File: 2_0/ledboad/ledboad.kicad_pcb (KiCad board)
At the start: 2 copper layers, 96 x 34.2 mm, 333 parts, among them J1 Conn_02x05_Odd_Even, Q1 AO3401A, Q2 AO3401A, Q3 AO3401A, Q4 AO3401A, Q5 AO3401A, Q6 AO3401A, Q7 AO3401A, Q8 AO3401A, SW1 RST, U1 STM32G070CBTx, U2 XC6206PxxxMR, Y1 2016/DNP

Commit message: save before next rev
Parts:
- added REF**: pilkbrain, Critbit_lib:pilkbrain, B.Cu at (62.0, 31.1)

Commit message: commit before rescheme
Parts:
- removed C1, C3: 100n, Capacitor_SMD:C_0402_1005Metric
- removed C2, C4: 470n, Capacitor_SMD:C_0402_1005Metric
- removed C7, C8: 10p/DNP, Capacitor_SMD:C_0402_1005Metric
- removed REF**: pilkbrain, Critbit_lib:pilkbrain
- removed SW1: RST, Button_Switch_SMD:SW_SPST_FSMSM
- removed TP1, TP10, TP11, TP12, TP13, TP14, TP15, TP16, TP17, TP18, TP19, TP2, TP20, TP21, TP22, TP23, TP24, TP25, TP26, TP27, TP28, TP29, TP3, TP30, TP31, TP32, TP4, TP5, TP6, TP7, TP8, TP9: TP, TestPoint:TestPoint_Pad_D1.0mm
- removed U1: STM32G070CBTx, Package_QFP:LQFP-48_7x7mm_P0.5mm
- removed Y1: 2016/DNP, Crystal:Crystal_SMD_2016-4Pin_2.0x1.6mm
- added R18: 5.1k, Resistor_SMD:R_0201_0603Metric, F.Cu at (93.7, 53.6)
- added R19: 5.1k, Resistor_SMD:R_0201_0603Metric, F.Cu at (91.8, 53.6)
- added U3: ~, Critbit_lib:pilkbrain, B.Cu at (55.8, 32.2)
- J1: value Conn_02x05_Odd_Even -> USB_C_Receptacle_USB2.0; footprint Critbit_lib:YXT-BB10-10S -> Connector_USB:USB_C_Receptacle_HRO_TYPE-C-31-M-12; moved to F.Cu
- U2: value XC6206PxxxMR -> 74HC138PW,118; footprint Package_TO_SOT_SMD:SOT-23-3 -> easyeda2kicad:SSOP-16_L6.2-W5.3-P0.65-LS7.8-BL
- moved J1 33.2 mm to (93.0, 46.4)
- moved U2 30.7 mm to (58.6, 55.8), turned to 0 degrees
- moved C5 8.66 mm to (72.0, 56.8), turned to 90 degrees
- moved C10 1.46 mm to (137.8, 48.6)
- moved D0_1 1.46 mm to (46.5, 17.9)
- moved D0_2 1.46 mm to (46.5, 20.8)
- moved D0_3 1.46 mm to (46.5, 23.8)
- moved D0_4 1.46 mm to (46.5, 26.8)
- moved D0_5 1.46 mm to (46.5, 29.8)
- moved D0_6 1.46 mm to (46.5, 32.8)
- moved D0_7 1.46 mm to (46.5, 35.8)
- moved D0_8 1.46 mm to (46.5, 38.8)
- moved D1 1.46 mm to (100.2, 46.0)
- moved D10_1 1.46 mm to (76.5, 17.9)
- moved D10_2 1.46 mm to (76.5, 20.8)
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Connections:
- RU6 pad 22: /DAT6 -> unconnected-(RU6-SDO-Pad22)
- U2 pad 1: GND -> /MATRIX_A
- U2 pad 2: +3V3 -> /MATRIX_B
- U2 pad 3: VDD -> /MATRIX_C
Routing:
- net /ROW_0_CTRL: track 67.2 -> 4.86 mm, vias 2 -> 1
- net /WS2812_DAT: track 45.1 -> 0.00 mm, vias 3 -> 0
- net VDD: track 195.9 -> 154.4 mm, vias 18 -> 15
- net /DAT0: track 44.2 -> 4.32 mm, vias 0 -> 1
- net /ROW_1_CTRL: track 46.5 -> 6.93 mm
- net GND: track 46.7 -> 21.0 mm, vias 17 -> 9
- net /OE: track 125.2 -> 100.4 mm, vias 12 -> 8
- net /LAT: track 119.6 -> 95.2 mm, vias 14 -> 11
- net /SCLK: track 93.6 -> 73.9 mm
- net /ROW_2_CTRL: track 24.9 -> 5.50 mm, vias 2 -> 0
- net /DM: track 0.00 -> 15.2 mm, vias 0 -> 2
- net /STM_NRST: track 14.2 -> 0.00 mm, vias 4 -> 0
- net +3V3: track 11.0 -> 0.00 mm, vias 1 -> 0
- net /ROW_3_CTRL: track 60.2 -> 50.3 mm, vias 4 -> 3
- net /STM_LEDB: track 9.66 -> 0.00 mm, vias 2 -> 0
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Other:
- board size 96 x 34.2 mm -> 100 x 32 mm
- board text added: "10.2024"
- board text added: "Cyberbadge 2.1"
- board text removed: "07.2023"
- board text removed: "Cyberbadge 2.0 prototype"
- board text removed: "D0 | LAT | 4x ext"
- board text removed: "D1"
- board text removed: "DAT2"
- board text removed: "DAT5"
- board text removed: "DAT6"
- board text removed: "GND"
- board text removed: "LAT | SCLK"
- board text removed: "OE"
- board text removed: "SPI2_MOSI | SPI2_MISO | OE | SPI2_SCLK"
- board text removed: "SPI2_NSS | SCLK | GND | ADC"
- board text removed: "SWCLK | SWDIO | GND | nRST | 3v3 | VDD | DAT3"
- board text removed: "TX | RX"

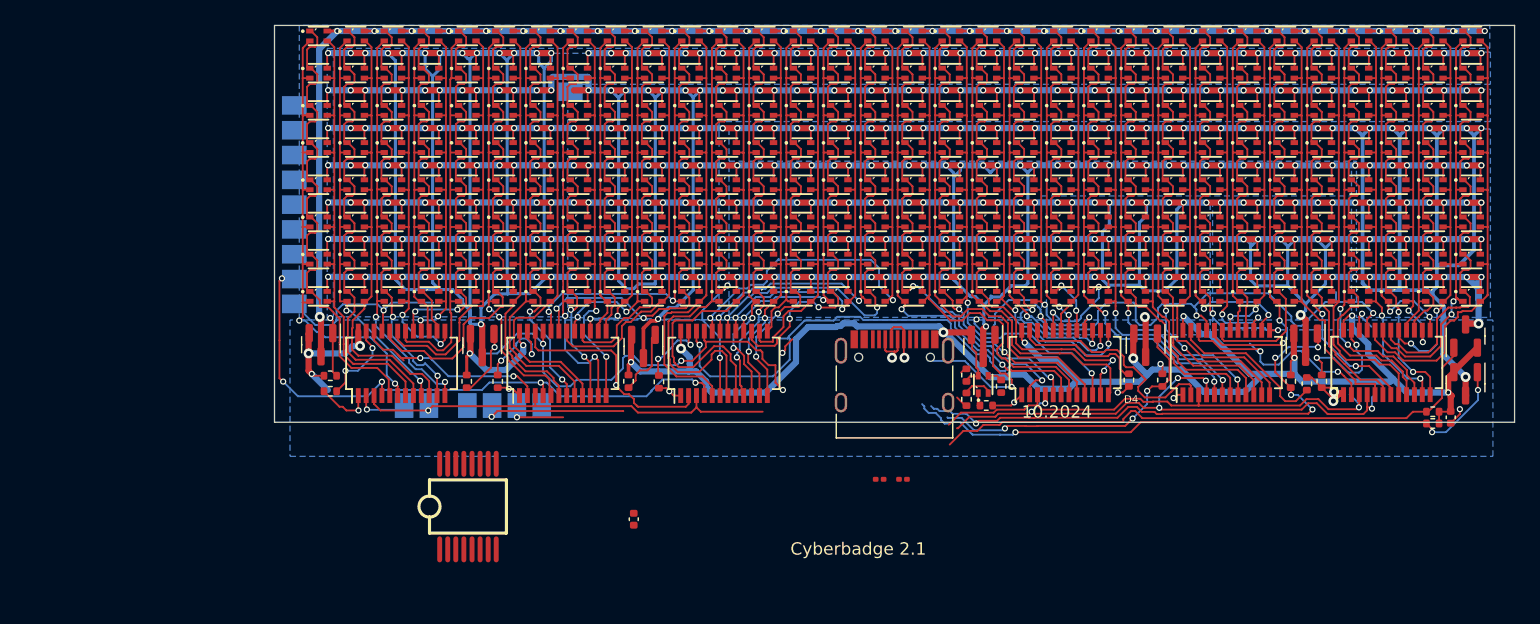
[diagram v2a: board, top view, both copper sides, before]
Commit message: rescheme, reroute
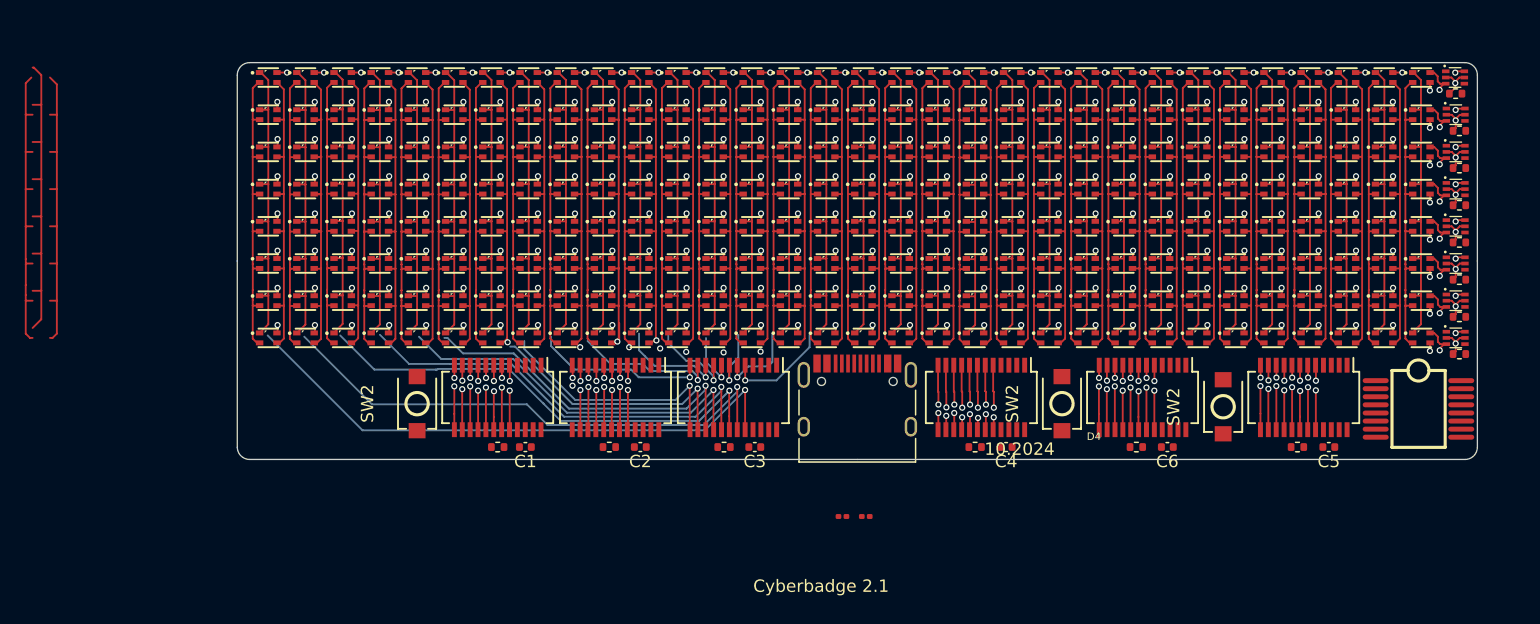
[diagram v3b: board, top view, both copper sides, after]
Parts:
- removed C10: 470n, Capacitor_SMD:C_0402_1005Metric
- removed D1: LED_RGBA, Critbit_lib:0606
- removed Q1, Q2, Q3, Q4, Q5, Q6, Q7, Q8: AO3401A, Package_TO_SOT_SMD:SOT-23
- removed R1, R2, R3, R4, R5, R6, R7, R8: 10k, Resistor_SMD:R_0402_1005Metric
- removed U3: ~, Critbit_lib:pilkbrain
- added C1: 470n, Capacitor_SMD:C_0402_1005Metric, F.Cu at (63.2, 51.0)
- added C2: 470n, Capacitor_SMD:C_0402_1005Metric, F.Cu at (72.5, 51.0)
- added C3: 470n, Capacitor_SMD:C_0402_1005Metric, F.Cu at (81.7, 51.0)
- added C4: 470n, Capacitor_SMD:C_0402_1005Metric, F.Cu at (102.0, 51.0)
- added C6: 470n, Capacitor_SMD:C_0402_1005Metric, F.Cu at (115.0, 51.0)
- added Q10: CJX3139K, easyeda2kicad:SOT-563_L1.6-W1.2-P0.50-LS1.6-BR, F.Cu at (138.2, 24.2)
- added Q11: CJX3139K, easyeda2kicad:SOT-563_L1.6-W1.2-P0.50-LS1.6-BR, F.Cu at (138.2, 27.2)
- added Q12: CJX3139K, easyeda2kicad:SOT-563_L1.6-W1.2-P0.50-LS1.6-BR, F.Cu at (138.2, 30.2)
- added Q13: CJX3139K, easyeda2kicad:SOT-563_L1.6-W1.2-P0.50-LS1.6-BR, F.Cu at (138.2, 33.2)
- added Q14: CJX3139K, easyeda2kicad:SOT-563_L1.6-W1.2-P0.50-LS1.6-BR, F.Cu at (138.2, 36.2)
- added Q15: CJX3139K, easyeda2kicad:SOT-563_L1.6-W1.2-P0.50-LS1.6-BR, F.Cu at (138.2, 39.2)
- added Q16: CJX3139K, easyeda2kicad:SOT-563_L1.6-W1.2-P0.50-LS1.6-BR, F.Cu at (138.2, 42.2)
- added Q9: CJX3139K, easyeda2kicad:SOT-563_L1.6-W1.2-P0.50-LS1.6-BR, F.Cu at (138.2, 21.2)
- added R20: 10k, Resistor_SMD:R_0402_1005Metric, F.Cu at (138.6, 31.5)
- added R21: 10k, Resistor_SMD:R_0402_1005Metric, F.Cu at (138.6, 34.5)
- added R22: 10k, Resistor_SMD:R_0402_1005Metric, F.Cu at (138.6, 37.5)
- added R23: 10k, Resistor_SMD:R_0402_1005Metric, F.Cu at (138.6, 40.5)
- added R24: 10k, Resistor_SMD:R_0402_1005Metric, F.Cu at (138.6, 43.5)
- added SW2: TS-1088-AR02016, easyeda2kicad:SW-SMD_L3.9-W3.0-P4.45, F.Cu at (54.5, 47.5)
- added SW2: TS-1088-AR02016, easyeda2kicad:SW-SMD_L3.9-W3.0-P4.45, F.Cu at (119.5, 47.8)
- added SW2: TS-1088-AR02016, easyeda2kicad:SW-SMD_L3.9-W3.0-P4.45, F.Cu at (106.5, 47.5)
- moved R9 78.1 mm to (125.5, 51.0), turned to 0 degrees
- moved U2 77.1 mm to (135.2, 47.9), turned to -90 degrees
- moved RU1 72.8 mm to (126.0, 47.0), turned to -90 degrees
- moved RU6 71.8 mm to (61.0, 47.0), turned to -90 degrees
- moved R14 66.7 mm to (61.0, 51.0), turned to 0 degrees
- moved R12 56.5 mm to (70.0, 51.0), turned to 0 degrees
- moved C5 56.4 mm to (128.0, 51.0), turned to 180 degrees
- moved R11 51.8 mm to (112.5, 51.0), turned to 0 degrees
- moved RU4 49.3 mm to (70.5, 47.0), turned to -90 degrees
- moved RU3 46.8 mm to (113.0, 47.0), turned to -90 degrees
- moved R15 45.4 mm to (138.2, 22.5), turned to 180 degrees
- moved R16 45.3 mm to (138.6, 25.5), turned to 180 degrees
- moved R17 40.9 mm to (138.6, 28.5), turned to 180 degrees
- moved R10 33.1 mm to (79.2, 51.0), turned to 0 degrees
- moved RU2 26.9 mm to (80.0, 47.0), turned to -90 degrees
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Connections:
- R15 pad 1: Net-(D1-RK) -> VDD
- R15 pad 2: GND -> /ROW_0_CTRL
- R16 pad 1: Net-(D1-GK) -> VDD
- R16 pad 2: /STM_LEDG -> /ROW_1_CTRL
- R17 pad 1: Net-(D1-BK) -> VDD
- R17 pad 2: /STM_LEDB -> /ROW_2_CTRL
- RU1 pad 10: /COL_B1 -> /COL_R26
- RU1 pad 11: /COL_R2 -> /COL_R25
- RU1 pad 12: /COL_G2 -> /COL_R24
- RU1 pad 13: /COL_B2 -> /COL_R23
- RU1 pad 14: /COL_R3 -> /COL_R22
- RU1 pad 15: /COL_G3 -> /COL_R21
- RU1 pad 16: /COL_B3 -> /COL_R20
- RU1 pad 17: /COL_R4 -> /COL_R19
- RU1 pad 18: /COL_G4 -> /COL_R18
- RU1 pad 19: /COL_B4 -> /COL_R17
- RU1 pad 2: /DAT0 -> /DAT_R
- RU1 pad 20: /COL_R5 -> /COL_R16
- RU1 pad 22: /DAT1 -> Net-(RU1-SDO)
- RU1 pad 5: /COL_R0 -> /COL_R31
- RU1 pad 6: /COL_G0 -> /COL_R30
- RU1 pad 7: /COL_B0 -> /COL_R29
- RU1 pad 8: /COL_R1 -> /COL_R28
- RU1 pad 9: /COL_G1 -> /COL_R27
- RU2 pad 10: /COL_B17 -> /COL_R10
- RU2 pad 11: /COL_R18 -> /COL_R9
- RU2 pad 12: /COL_G18 -> /COL_R8
- RU2 pad 13: /COL_B18 -> /COL_R7
- RU2 pad 14: /COL_R19 -> /COL_R6
- RU2 pad 15: /COL_G19 -> /COL_R5
- RU2 pad 16: /COL_B19 -> /COL_R4
- RU2 pad 17: /COL_R20 -> /COL_R3
- RU2 pad 18: /COL_G20 -> /COL_R2
- RU2 pad 19: /COL_B20 -> /COL_R1
- RU2 pad 2: /DAT3 -> Net-(RU1-SDO)
- RU2 pad 20: /COL_R21 -> /COL_R0
- RU2 pad 22: /DAT4 -> unconnected-(RU2-SDO-Pad22)
- RU2 pad 5: /COL_R16 -> /COL_R15
- RU2 pad 6: /COL_G16 -> /COL_R14
- RU2 pad 7: /COL_B16 -> /COL_R13
- RU2 pad 8: /COL_R17 -> /COL_R12
- RU2 pad 9: /COL_G17 -> /COL_R11
- RU3 pad 10: /COL_R7 -> /COL_G26
- RU3 pad 11: /COL_G7 -> /COL_G25
- RU3 pad 12: /COL_B7 -> /COL_G24
- RU3 pad 13: /COL_R8 -> /COL_G23
- RU3 pad 14: /COL_G8 -> /COL_G22
- RU3 pad 15: /COL_B8 -> /COL_G21
- RU3 pad 16: /COL_R9 -> /COL_G20
- RU3 pad 17: /COL_G9 -> /COL_G19
- RU3 pad 18: /COL_B9 -> /COL_G18
- RU3 pad 19: /COL_R10 -> /COL_G17
- RU3 pad 2: /DAT1 -> /DAT_G
- RU3 pad 20: /COL_G10 -> /COL_G16
- RU3 pad 22: /DAT2 -> Net-(RU3-SDO)
- RU3 pad 5: /COL_G5 -> /COL_G31
- RU3 pad 6: /COL_B5 -> /COL_G30
- RU3 pad 7: /COL_R6 -> /COL_G29
- RU3 pad 8: /COL_G6 -> /COL_G28
- RU3 pad 9: /COL_B6 -> /COL_G27
- RU4 pad 10: /COL_R23 -> /COL_G10
- RU4 pad 11: /COL_G23 -> /COL_G9
- RU4 pad 12: /COL_B23 -> /COL_G8
- RU4 pad 13: /COL_R24 -> /COL_G7
- RU4 pad 14: /COL_G24 -> /COL_G6
- RU4 pad 15: /COL_B24 -> /COL_G5
- RU4 pad 16: /COL_R25 -> /COL_G4
- RU4 pad 17: /COL_G25 -> /COL_G3
- RU4 pad 18: /COL_B25 -> /COL_G2
- RU4 pad 19: /COL_R26 -> /COL_G1
- RU4 pad 2: /DAT4 -> Net-(RU3-SDO)
- RU4 pad 20: /COL_G26 -> /COL_G0
- RU4 pad 22: /DAT5 -> unconnected-(RU4-SDO-Pad22)
- RU4 pad 5: /COL_G21 -> /COL_G15
- RU4 pad 6: /COL_B21 -> /COL_G14
- RU4 pad 7: /COL_R22 -> /COL_G13
- RU4 pad 8: /COL_G22 -> /COL_G12
- RU4 pad 9: /COL_B22 -> /COL_G11
- RU5 pad 10: /COL_G12 -> /COL_B26
- RU5 pad 11: /COL_B12 -> /COL_B25
- RU5 pad 12: /COL_R13 -> /COL_B24
- RU5 pad 13: /COL_G13 -> /COL_B23
- RU5 pad 14: /COL_B13 -> /COL_B22
- RU5 pad 15: /COL_R14 -> /COL_B21
- RU5 pad 16: /COL_G14 -> /COL_B20
- RU5 pad 17: /COL_B14 -> /COL_B19
- RU5 pad 18: /COL_R15 -> /COL_B18
- RU5 pad 19: /COL_G15 -> /COL_B17
- RU5 pad 2: /DAT2 -> /DAT_B
- RU5 pad 20: /COL_B15 -> /COL_B16
- RU5 pad 22: /DAT3 -> Net-(RU5-SDO)
- RU5 pad 5: /COL_B10 -> /COL_B31
- RU5 pad 6: /COL_R11 -> /COL_B30
- RU5 pad 7: /COL_G11 -> /COL_B29
- RU5 pad 8: /COL_B11 -> /COL_B28
- RU5 pad 9: /COL_R12 -> /COL_B27
- RU6 pad 10: /COL_G28 -> /COL_B10
- RU6 pad 11: /COL_B28 -> /COL_B9
- RU6 pad 12: /COL_R29 -> /COL_B8
- RU6 pad 13: /COL_G29 -> /COL_B7
- RU6 pad 14: /COL_B29 -> /COL_B6
- RU6 pad 15: /COL_R30 -> /COL_B5
- RU6 pad 16: /COL_G30 -> /COL_B4
- RU6 pad 17: /COL_B30 -> /ROW_7
- RU6 pad 18: /COL_R31 -> /COL_B2
- RU6 pad 19: /COL_G31 -> /COL_B1
- RU6 pad 2: /DAT5 -> Net-(RU5-SDO)
- RU6 pad 20: /COL_B31 -> /COL_B0
- RU6 pad 5: /COL_B26 -> /COL_B15
- RU6 pad 6: /COL_R27 -> /COL_B14
- RU6 pad 7: /COL_G27 -> /COL_B13
- RU6 pad 8: /COL_B27 -> /COL_B12
- RU6 pad 9: /COL_R28 -> /COL_B11
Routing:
- net /ROW_1: track 251.3 -> 23.1 mm, vias 63 -> 33
- net /ROW_3: track 203.5 -> 23.1 mm, vias 64 -> 33
- net /ROW_2: track 195.0 -> 23.1 mm, vias 63 -> 33
- net VDD: track 154.4 -> 0.00 mm, vias 15 -> 0
- net /ROW_4: track 166.5 -> 23.1 mm, vias 64 -> 33
- net /ROW_5: track 161.1 -> 23.1 mm, vias 64 -> 33
- net /ROW_6: track 158.0 -> 23.1 mm, vias 64 -> 33
- net /ROW_0: track 145.4 -> 27.2 mm
- net /OE: track 100.4 -> 0.00 mm, vias 8 -> 0
- net /ROW_7: track 138.5 -> 40.6 mm, vias 64 -> 34
- net /LAT: track 95.2 -> 0.00 mm, vias 11 -> 0
- net /SCLK: track 73.9 -> 0.00 mm, vias 2 -> 0
- net /COL_R0: track 40.6 -> 97.8 mm, vias 0 -> 1
- net /COL_G0: track 38.9 -> 85.6 mm, vias 2 -> 1
- net /DAT3: track 39.9 -> 0.00 mm, vias 2 -> 0
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- added copper zone on In1.Cu, net /ROW_0
- added copper zone on In1.Cu, net /ROW_1
- added copper zone on In1.Cu, net /ROW_2
- added copper zone on In1.Cu, net /ROW_3
- added copper zone on In1.Cu, net /ROW_4
- added copper zone on In1.Cu, net /ROW_5
- added copper zone on In1.Cu, net /ROW_6
- added copper zone on In1.Cu, net /ROW_7
- removed copper zone on B.Cu, net /ROW_0
- removed copper zone on B.Cu, net /ROW_1
- removed copper zone on B.Cu, net /ROW_2
- removed copper zone on B.Cu, net /ROW_3
- removed copper zone on B.Cu, net /ROW_4
- removed copper zone on B.Cu, net /ROW_5
- removed copper zone on B.Cu, net /ROW_6
- removed copper zone on B.Cu, net GND
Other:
- outline, holes or cut-outs redrawn
- copper layers 2 -> 4

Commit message: work on ledboard
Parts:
- removed the SW2 at (54.5, 47.5)
- removed the SW2 at (119.5, 47.8)
- added C7: 470n, Capacitor_SMD:C_0402_1005Metric, F.Cu at (138.9, 43.6)
- added SW1: TS-1088-AR02016, easyeda2kicad:SW-SMD_L3.9-W3.0-P4.45, F.Cu at (119.5, 47.3)
- added SW3: TS-1088-AR02016, easyeda2kicad:SW-SMD_L3.9-W3.0-P4.45, F.Cu at (51.9, 47.0)
- added U1: ~, Critbit_lib:pilkbrain2, B.Cu at (53.4, 38.8)
- R18, R19: footprint Resistor_SMD:R_0201_0603Metric -> Resistor_SMD:R_0402_1005Metric
- moved C5 33.6 mm to (95.3, 43.5)
- moved C6 16.5 mm to (131.5, 50.2), turned to 0 degrees
- moved R18 14.2 mm to (84.2, 44.0), turned to -90 degrees
- moved R19 11.6 mm to (84.2, 45.9), turned to 90 degrees
- moved R9 9.53 mm to (131.5, 43.6)
- moved R11 9.44 mm to (118.6, 43.8)
- moved R13 9.44 mm to (105.6, 43.8)
- moved C4 9.06 mm to (107.5, 43.8)
- moved R10 7.81 mm to (73.8, 45.4), turned to 90 degrees
- moved R24 6.70 mm to (138.8, 50.2)
- moved R12 5.23 mm to (73.8, 47.4), turned to -90 degrees
- moved R14 4.15 mm to (63.2, 47.5), turned to -90 degrees
- moved RU6 3.00 mm to (58.0, 47.0)
- moved C3 2.84 mm to (84.2, 49.6), turned to 90 degrees
- moved C2 2.06 mm to (73.8, 49.4), turned to 90 degrees
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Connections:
- RU1 pad 10: /COL_R26 -> /COL_R21
- RU1 pad 11: /COL_R25 -> /COL_R22
- RU1 pad 12: /COL_R24 -> /COL_R23
- RU1 pad 13: /COL_R23 -> /COL_R24
- RU1 pad 14: /COL_R22 -> /COL_R25
- RU1 pad 15: /COL_R21 -> /COL_R26
- RU1 pad 16: /COL_R20 -> /COL_R27
- RU1 pad 17: /COL_R19 -> /COL_R28
- RU1 pad 18: /COL_R18 -> /COL_R29
- RU1 pad 19: /COL_R17 -> /COL_R30
- RU1 pad 2: /DAT_R -> Net-(RU1-SDI)
- RU1 pad 20: /COL_R16 -> /COL_R31
- RU1 pad 22: Net-(RU1-SDO) -> unconnected-(RU1-SDO-Pad22)
- RU1 pad 5: /COL_R31 -> /COL_R16
- RU1 pad 6: /COL_R30 -> /COL_R17
- RU1 pad 7: /COL_R29 -> /COL_R18
- RU1 pad 8: /COL_R28 -> /COL_R19
- RU1 pad 9: /COL_R27 -> /COL_R20
- RU2 pad 10: /COL_R10 -> /COL_R5
- RU2 pad 11: /COL_R9 -> /COL_R6
- RU2 pad 12: /COL_R8 -> /COL_R7
- RU2 pad 13: /COL_R7 -> /COL_R8
- RU2 pad 14: /COL_R6 -> /COL_R9
- RU2 pad 15: /COL_R5 -> /COL_R10
- RU2 pad 16: /COL_R4 -> /COL_R11
- RU2 pad 17: /COL_R3 -> /COL_R12
- RU2 pad 18: /COL_R2 -> /COL_R13
- RU2 pad 19: /COL_R1 -> /COL_R14
- RU2 pad 2: Net-(RU1-SDO) -> /DAT_R
- RU2 pad 20: /COL_R0 -> /COL_R15
- RU2 pad 22: unconnected-(RU2-SDO-Pad22) -> Net-(RU1-SDI)
- RU2 pad 5: /COL_R15 -> /COL_R0
- RU2 pad 6: /COL_R14 -> /COL_R1
- RU2 pad 7: /COL_R13 -> /COL_R2
- RU2 pad 8: /COL_R12 -> /COL_R3
- RU2 pad 9: /COL_R11 -> /COL_R4
- RU3 pad 10: /COL_G26 -> /COL_G21
- RU3 pad 11: /COL_G25 -> /COL_G22
- RU3 pad 12: /COL_G24 -> /COL_G23
- RU3 pad 13: /COL_G23 -> /COL_G24
- RU3 pad 14: /COL_G22 -> /COL_G25
- RU3 pad 15: /COL_G21 -> /COL_G26
- RU3 pad 16: /COL_G20 -> /COL_G27
- RU3 pad 17: /COL_G19 -> /COL_G28
- RU3 pad 18: /COL_G18 -> /COL_G29
- RU3 pad 19: /COL_G17 -> /COL_G30
- RU3 pad 2: /DAT_G -> Net-(RU3-SDI)
- RU3 pad 20: /COL_G16 -> /COL_G31
- RU3 pad 22: Net-(RU3-SDO) -> unconnected-(RU3-SDO-Pad22)
- RU3 pad 5: /COL_G31 -> /COL_G16
- RU3 pad 6: /COL_G30 -> /COL_G17
- RU3 pad 7: /COL_G29 -> /COL_G18
- RU3 pad 8: /COL_G28 -> /COL_G19
- RU3 pad 9: /COL_G27 -> /COL_G20
- RU4 pad 10: /COL_G10 -> /COL_G5
- RU4 pad 11: /COL_G9 -> /COL_G6
- RU4 pad 12: /COL_G8 -> /COL_G7
- RU4 pad 13: /COL_G7 -> /COL_G8
- RU4 pad 14: /COL_G6 -> /COL_G9
- RU4 pad 15: /COL_G5 -> /COL_G10
- RU4 pad 16: /COL_G4 -> /COL_G11
- RU4 pad 17: /COL_G3 -> /COL_G12
- RU4 pad 18: /COL_G2 -> /COL_G13
- RU4 pad 19: /COL_G1 -> /COL_G14
- RU4 pad 2: Net-(RU3-SDO) -> /DAT_G
- RU4 pad 20: /COL_G0 -> /COL_G15
- RU4 pad 22: unconnected-(RU4-SDO-Pad22) -> Net-(RU3-SDI)
- RU4 pad 5: /COL_G15 -> /COL_G0
- RU4 pad 6: /COL_G14 -> /COL_G1
- RU4 pad 7: /COL_G13 -> /COL_G2
- RU4 pad 8: /COL_G12 -> /COL_G3
- RU4 pad 9: /COL_G11 -> /COL_G4
- RU5 pad 10: /COL_B26 -> /COL_B21
- RU5 pad 11: /COL_B25 -> /COL_B22
- RU5 pad 12: /COL_B24 -> /COL_B23
- RU5 pad 13: /COL_B23 -> /COL_B24
- RU5 pad 14: /COL_B22 -> /COL_B25
- RU5 pad 15: /COL_B21 -> /COL_B26
- RU5 pad 16: /COL_B20 -> /COL_B27
- RU5 pad 17: /COL_B19 -> /COL_B28
- RU5 pad 18: /COL_B18 -> /COL_B29
- RU5 pad 19: /COL_B17 -> /COL_B30
- RU5 pad 2: /DAT_B -> Net-(RU5-SDI)
- RU5 pad 20: /COL_B16 -> /COL_B31
- RU5 pad 22: Net-(RU5-SDO) -> unconnected-(RU5-SDO-Pad22)
- RU5 pad 5: /COL_B31 -> /COL_B16
- RU5 pad 6: /COL_B30 -> /COL_B17
- RU5 pad 7: /COL_B29 -> /COL_B18
- RU5 pad 8: /COL_B28 -> /COL_B19
- RU5 pad 9: /COL_B27 -> /COL_B20
- RU6 pad 10: /COL_B10 -> /COL_B5
- RU6 pad 11: /COL_B9 -> /COL_B6
- RU6 pad 12: /COL_B8 -> /COL_B7
- RU6 pad 13: /COL_B7 -> /COL_B8
- RU6 pad 14: /COL_B6 -> /COL_B9
- RU6 pad 15: /COL_B5 -> /COL_B10
- RU6 pad 16: /COL_B4 -> /COL_B11
- RU6 pad 17: /ROW_7 -> /COL_B12
- RU6 pad 18: /COL_B2 -> /COL_B13
- RU6 pad 19: /COL_B1 -> /COL_B14
- RU6 pad 2: Net-(RU5-SDO) -> /DAT_B
- RU6 pad 20: /COL_B0 -> /COL_B15
- RU6 pad 22: unconnected-(RU6-SDO-Pad22) -> Net-(RU5-SDI)
- RU6 pad 5: /COL_B15 -> /COL_B0
- RU6 pad 6: /COL_B14 -> /COL_B1
- RU6 pad 7: /COL_B13 -> /COL_B2
- RU6 pad 8: /COL_B12 -> /COL_B3
- RU6 pad 9: /COL_B11 -> /COL_B4
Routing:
- net /MATRIX_C: track 0.00 -> 119.8 mm, vias 0 -> 1
- net /MATRIX_B: track 0.00 -> 116.0 mm, vias 0 -> 1
- net /MATRIX_A: track 0.00 -> 110.9 mm, vias 0 -> 1
- net /LAT: track 0.00 -> 101.9 mm, vias 0 -> 6
- net /SCLK: track 0.00 -> 93.5 mm, vias 0 -> 1
- net /OE: track 0.00 -> 79.6 mm, vias 0 -> 4
- net Net-(RU1-SDI): track 0.00 -> 55.4 mm, vias 0 -> 2
- net VDD: track 0.00 -> 52.6 mm, vias 0 -> 8
- net /DAT_R: track 0.00 -> 47.4 mm, vias 0 -> 1
- net /COL_R16: track 29.0 -> 75.6 mm, vias 1 -> 2
- net Net-(RU3-SDI): track 0.00 -> 45.1 mm, vias 0 -> 2
- net /COL_R17: track 29.2 -> 72.3 mm, vias 1 -> 2
- net /COL_B31: track 29.7 -> 70.8 mm
- net Net-(RU5-SDI): track 0.00 -> 39.8 mm, vias 0 -> 2
- net /COL_R18: track 28.9 -> 68.1 mm, vias 1 -> 2
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- added copper zone on In2.Cu, net GND
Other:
- board size 100 x 32 mm -> 100 x 30.8 mm

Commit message: before oder
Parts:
- added C10: 470n, Capacitor_SMD:C_0402_1005Metric, F.Cu at (51.7, 43.5)
- added C8: 470n, Capacitor_SMD:C_0402_1005Metric, F.Cu at (49.8, 43.5)
- added C9: 470n, Capacitor_SMD:C_0402_1005Metric, F.Cu at (120.4, 43.8)
- added JP1: SB, Jumper:SolderJumper-2_P1.3mm_Bridged_RoundedPad1.0x1.5mm, B.Cu at (131.4, 44.9)
- added JP2: SB, Jumper:SolderJumper-2_P1.3mm_Bridged_RoundedPad1.0x1.5mm, B.Cu at (131.4, 47.2)
- added JP3: SB, Jumper:SolderJumper-2_P1.3mm_Bridged_RoundedPad1.0x1.5mm, B.Cu at (131.4, 49.5)
- moved R24 9.70 mm to (138.5, 40.5)
- moved R23 9.70 mm to (138.7, 50.2), turned to 0 degrees
- moved U1 0.35 mm to (53.0, 38.8)
- turned SW1 to 90 degrees
- turned SW2 to 90 degrees
- turned SW3 to -90 degrees
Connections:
- SW1 pad 1: unconnected-(SW1-Pad1) -> /B1
- SW1 pad 2: unconnected-(SW1-Pad2) -> GND
- SW2 pad 1: unconnected-(SW2-Pad1) -> /B2
- SW2 pad 2: unconnected-(SW2-Pad2) -> GND
- SW3 pad 2: unconnected-(SW3-Pad2) -> GND
- U1 pad 5V: unconnected-(U1-5V_IN-Pad5V) -> VBUS
- U1 pad DM: unconnected-(U1-USB_DM-PadDM) -> /DM
- U1 pad DP: unconnected-(U1-USB_DP-PadDP) -> /DP
- U1 pad SCL: unconnected-(U1-PadSCL) -> /B2
- U1 pad SDA: unconnected-(U1-PadSDA) -> /B1
- U2 pad 4: unconnected-(U2-~{E1}-Pad4) -> Net-(JP1-A)
- U2 pad 5: unconnected-(U2-~{E2}-Pad5) -> Net-(JP2-A)
- U2 pad 6: unconnected-(U2-E3-Pad6) -> Net-(JP3-A)
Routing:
- net /B1: track 0.00 -> 88.4 mm, vias 0 -> 5
- net VDD: track 52.6 -> 127.8 mm, vias 8 -> 19
- net /B2: track 0.00 -> 73.7 mm, vias 0 -> 3
- net GND: track 35.4 -> 89.1 mm, vias 6 -> 19
- net VBUS: track 0.00 -> 38.0 mm, vias 0 -> 2
- net /OE: track 79.6 -> 113.8 mm, vias 4 -> 6
- net /DM: track 2.85 -> 32.7 mm, vias 0 -> 1
- net /DP: track 3.00 -> 32.4 mm, vias 0 -> 1
- net /COL_R0: track 98.7 -> 69.5 mm
- net /LAT: track 101.9 -> 129.8 mm, vias 6 -> 7
- net /COL_B0: track 69.7 -> 44.3 mm
- net /COL_G0: track 83.4 -> 59.3 mm
- net /COL_G28: track 26.2 -> 40.2 mm, vias 1 -> 0
- net Net-(RU3-REXT): track 0.00 -> 9.47 mm, vias 0 -> 2
- net unconnected-(U1-USB_DP-PadDP): track 6.99 -> 0.00 mm
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- added copper zone on B.Cu, net VDD
